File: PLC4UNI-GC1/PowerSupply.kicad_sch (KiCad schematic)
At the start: 6 parts, among them U3 PS-TO220

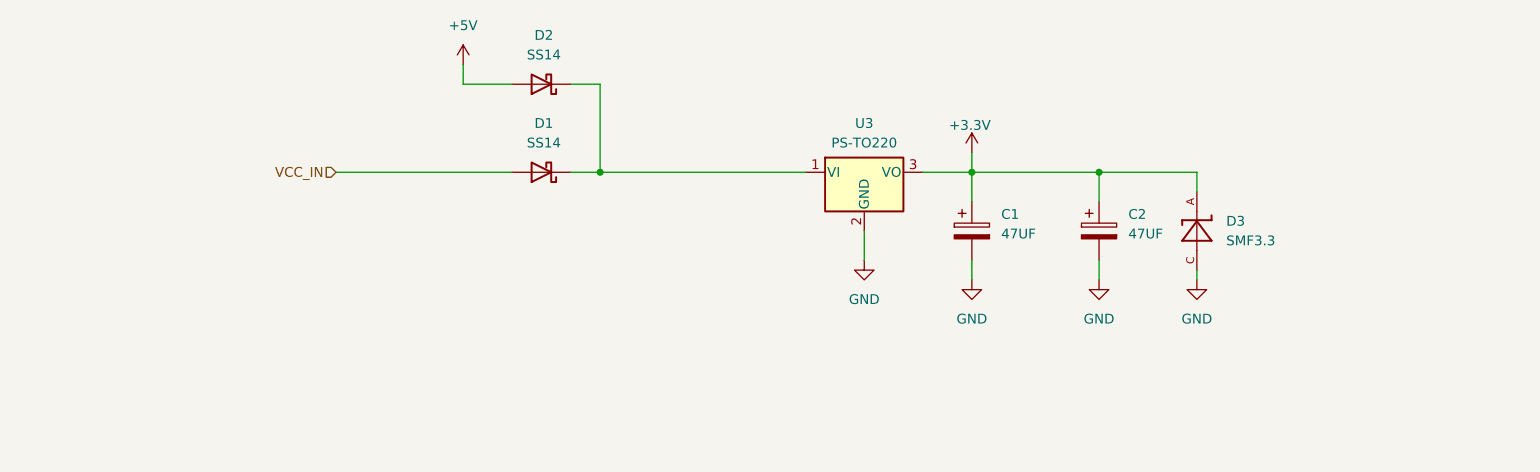
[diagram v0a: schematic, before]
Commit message: Colocadas el 80% de las piezas
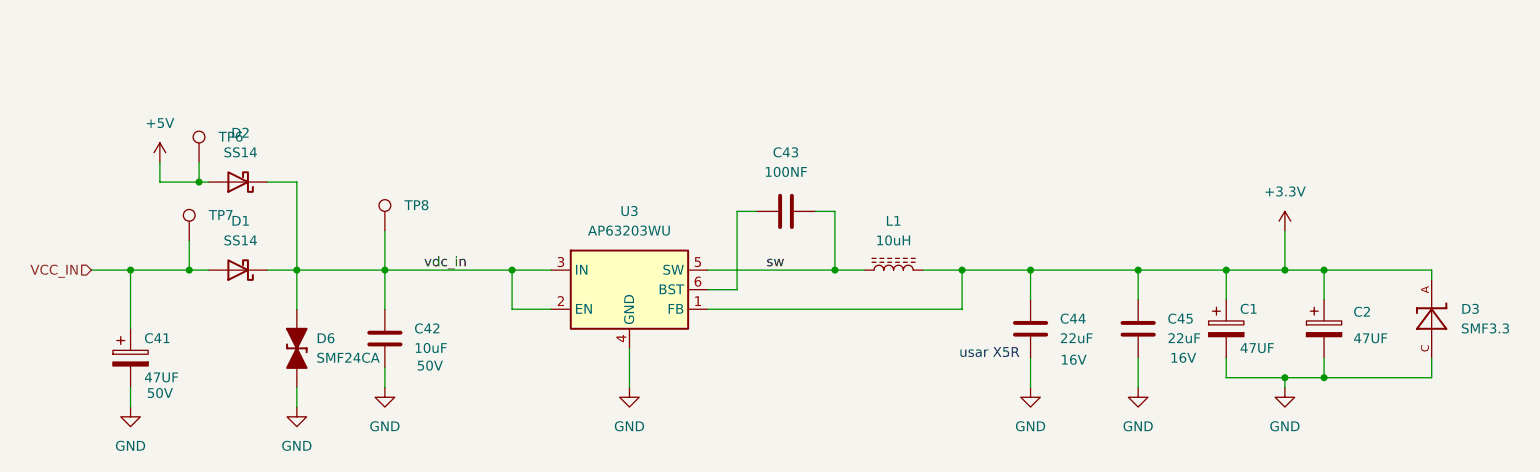
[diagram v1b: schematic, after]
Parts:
- removed U3: PS-TO220, MG_footprints:PS-TO-220-3_Vertical, symbol MG_IC:PS-TO220
- added C41: 47UF, Capacitor_SMD:CP_Elec_6.3x7.7, symbol MG_CAPACITOR:CAP-POL-SMD-47UF-16V-D6.3MM
- added C42: 10uF, Capacitor_SMD_AKL:C_0805_2012Metric, symbol Capacitor_AKL:C_0805
- added C43: 100NF, Capacitor_SMD_AKL:C_0805_2012Metric, symbol Capacitor_AKL:C_0805
- added C44, C45: 22uF, Capacitor_SMD_AKL:C_0805_2012Metric, symbol Capacitor_AKL:C_0805
- added D6: SMF24CA, Diode_SMD_AKL:D_SOD-123F, symbol Diode_TVS_AKL:SMF24CA
- added L1: 10uH, Inductor_SMD:L_APV_APH0630, symbol Device:L_Ferrite
- added TP6, TP7, TP8: TestPoint_Hole1, 4ms_TestPoint:TestPoint_WireHole, symbol MG_ELECTROMECANICAL:TestPoint_Hole1
- added U3: AP63203WU, Package_TO_SOT_SMD:TSOT-23-6, symbol Regulator_Switching:AP63203WU
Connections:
- net +3.3V: now also C44.1, C45.1, L1.2, U3.1 (FB)
- net +5V: now also TP6.1
- net GND: now also C41.2, C42.2, C44.2, C45.2, D6.1 (K), U3.4 (GND)
- net VCC_IN: now also C41.1, TP7.1
- net vdc_in: now reaches D1.1 (K), D2.1 (K)
- net vdc_in: now also C42.1, D6.2 (A), TP8.1, U3.2 (EN), U3.3 (IN)
- new net: C43.1, U3.6 (BST)
- new net sw: C43.2, L1.1, U3.5 (SW)
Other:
- note added: "usar X5R"
- moved on the sheet: C1, C2, D1, D2
